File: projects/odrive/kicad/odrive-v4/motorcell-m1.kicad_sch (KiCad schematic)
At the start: 57 parts, among them J3 M1 A/B/C, Q30 NVMFS5C628NL, Q31 NVMFS5C628NL, Q32 NVMFS5C628NL, Q33 NVMFS5C628NL, Q34 NVMFS5C628NL, Q35 NVMFS5C628NL, Q36 NVMFS5C628NL, Q37 NVMFS5C628NL, Q38 NVMFS5C628NL, Q39 NVMFS5C628NL, Q40 NVMFS5C628NL, Q41 NVMFS5C628NL, U4 DRV8353RS

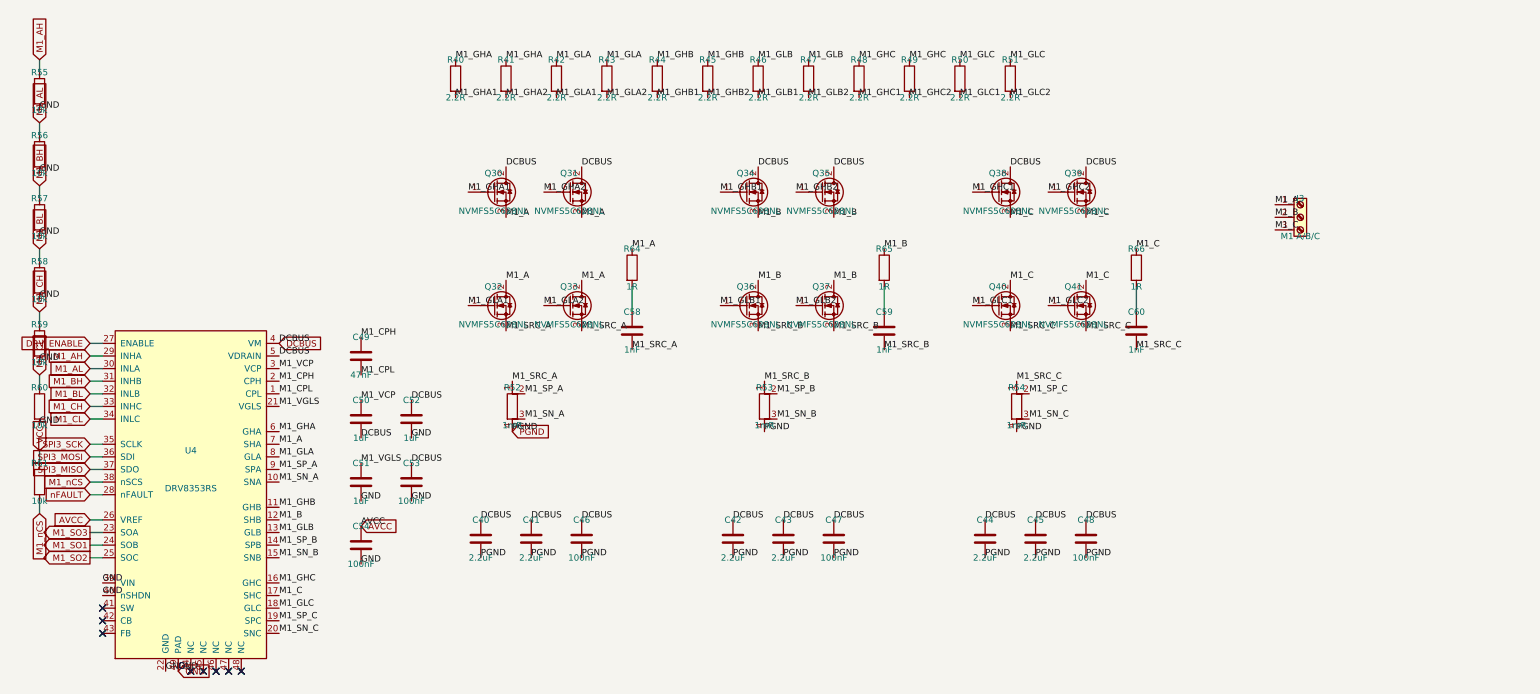
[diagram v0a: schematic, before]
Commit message: Make the v4 schematic sheets readable, netlist-invariant
The verified v4 schematic was electrically perfect and visually unreadable:
connectivity lived in labels stuck on pins, text overlapped, and parts sat
on the title block. Reworked all ten block sheets through Konnect: real
wires for local connections, labels kept for power rails and inter-sheet
nets, parts grouped by function, junction dots where wires join.

The invariant was enforced, not assumed: the exported netlist is diffed
against a reference frozen before the rework - 378 components and 283 nets,
identical membership pin by pin - and ERC holds at 0 errors. The lesson
that forced the rework is now a standing gate: numeric oracles (ERC,
netlist diff, overlap counts) all passed on the unreadable version, so
every sheet is also rendered to PNG and looked at before being declared
done.

An interrupted fix round left one known cosmetic issue, documented in
docs/LOG.md: the encoders-gpio GPIO group's reference/value text fields
float ~134mm right of their symbols, over the title block. konnect 0.2.2
has no tool that repositions property fields, so it waits for 0.11.0.
Also adds the fab footprints the sheets reference (MEGA fuse, Phoenix
terminal blocks, CMC) and restores the board file to the blank template -
the aborted layout skeleton was not worth keeping.
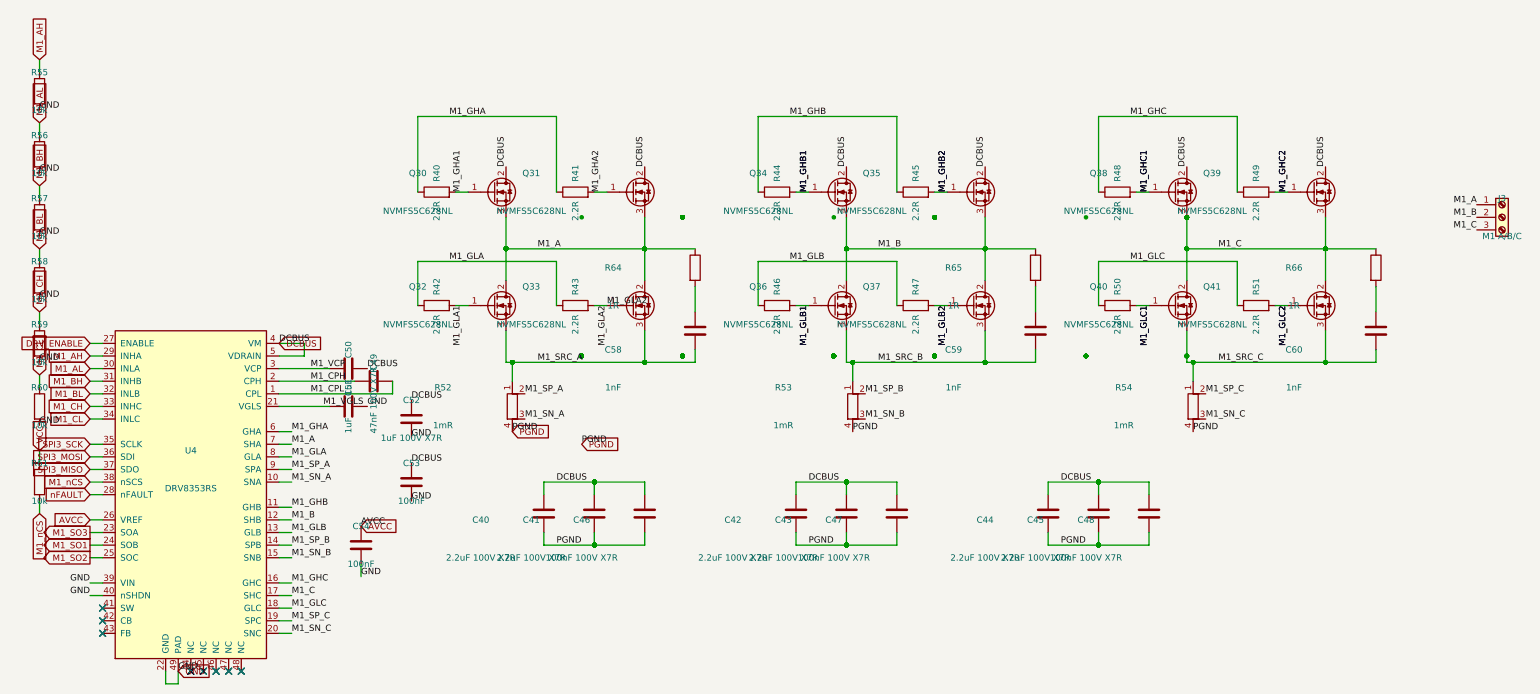
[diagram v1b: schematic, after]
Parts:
- C40, C41, C42, C43, C44, C45: value 2.2uF -> 2.2uF 100V X7R; footprint (none) -> Capacitor_SMD:C_1210_3225Metric
- C46, C47, C48: value 100nF -> 100nF 100V X7R; footprint (none) -> Capacitor_SMD:C_0603_1608Metric
- C49: value 47nF -> 47nF 100V X7R; footprint (none) -> Capacitor_SMD:C_0805_2012Metric
- C50, C51, C53, C54, C58, C59, C60: footprint (none) -> Capacitor_SMD:C_0603_1608Metric
- C52: value 1uF -> 1uF 100V X7R; footprint (none) -> Capacitor_SMD:C_1210_3225Metric
- J3: footprint (none) -> odrive_footprints:TerminalBlock_Phoenix_PC-16-3-ST-10.16mm
- Q30, Q31, Q32, Q33, Q34, Q35, Q36, Q37, Q38, Q39, Q40, Q41: footprint (none) -> Package_SO:PowerPAK_SO-8_Single
- R40, R41, R42, R43, R44, R45, R46, R47, R48, R49, R50, R51, R55, R56, R57, R58, R59, R60, R61, R64, R65, R66: footprint (none) -> Resistor_SMD:R_0603_1608Metric
- R52, R53, R54: footprint (none) -> Resistor_SMD:R_Shunt_Vishay_WSK2512_6332Metric_T1_T2
- U4: footprint (none) -> Package_DFN_QFN:QFN-48-1EP_7x7mm_P0.5mm_EP5.15x5.15mm_ThermalVias
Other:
- moved on the sheet: C40, C41, C42, C43, C44, C45, C46, C47, C48, C49, C50, C51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
